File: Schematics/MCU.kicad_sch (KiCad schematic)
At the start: 28 parts, among them J1 Microsemi_FlashPro-JTAG-10, U1 STM32F405RGT6, Y1 8mhz

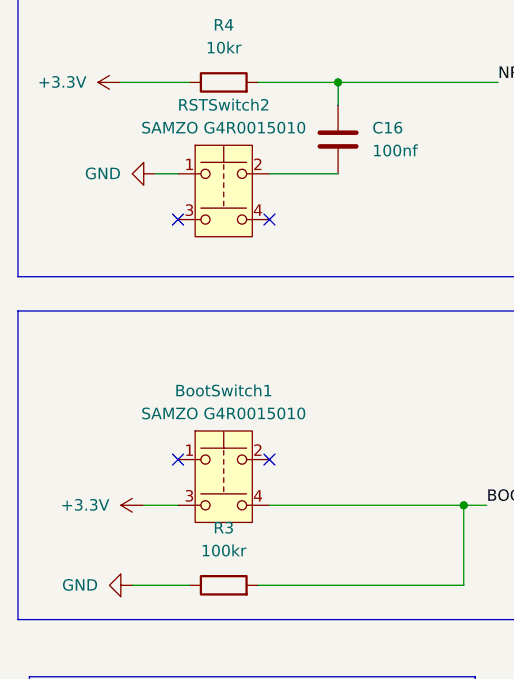
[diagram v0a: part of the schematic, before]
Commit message: fixed switch layout and unrouted nets
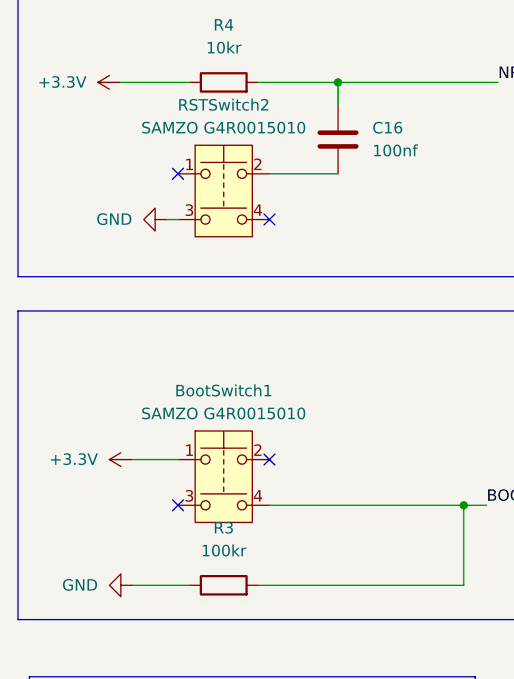
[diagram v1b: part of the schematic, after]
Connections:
- net +3.3V: now also BootSwitch1.1; no longer BootSwitch1.3
- net GND: now also RSTSwitch2.3; no longer RSTSwitch2.1
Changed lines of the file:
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@@
 	)
 	(no_connect
-		(at 33.02 95.25)
-	)
-	(no_connect
 		(at 127 96.52)
 	)
@@
 	)
 	(no_connect
+		(at 33.02 63.5)
+	)
+	(no_connect
 		(at 252.73 54.61)
 	)
@@
 	)
 	(no_connect
-		(at 33.02 68.58)
-	)
-	(no_connect
 		(at 127 121.92)
 	)
@@
 	)
 	(no_connect
+		(at 33.02 100.33)
+	)
+	(no_connect
 		(at 240.03 34.29)
 	)
@@
 	(wire
 		(pts
-			(xy 29.21 100.33) (xy 33.02 100.33)
+			(xy 29.21 157.48) (xy 31.75 157.48)
 		)
 		(stroke
@@
 	(wire
 		(pts
-			(xy 29.21 157.48) (xy 31.75 157.48)
+			(xy 31.75 68.58) (xy 33.02 68.58)
 		)
 		(stroke
@@
 	(wire
 		(pts
-			(xy 30.48 63.5) (xy 33.02 63.5)
-		)
-		(stroke
-			(width 0)
-			(type default)
-		)
-	)
-	(wire
-		(pts
 			(xy 153.67 31.75) (xy 160.02 31.75)
 		)
@@
 	(wire
 		(pts
+			(xy 27.94 95.25) (xy 33.02 95.25)
+		)
+		(stroke
+			(width 0)
+			(type default)
+		)
+	)
+	(wire
+		(pts
 			(xy 137.16 24.13) (xy 139.7 24.13)
 		)
@@
 	(symbol
 		(lib_id "power:+3.3V")
-		(at 29.21 100.33 90)
+		(at 27.94 95.25 90)
 		(unit 1)
 		(exclude_from_sim no)
@@
 		(fields_autoplaced yes)
 		(property "Reference" "#PWR017"
-			(at 33.02 100.33 0)
+			(at 31.75 95.25 0)
 			(effects
 				(font
@@
 		)
 		(property "Value" "+3.3V"
-			(at 25.4 100.3299 90)
+			(at 24.13 95.2499 90)
 			(effects
 				(font
@@
 		)
 		(property "Footprint" ""
-			(at 29.21 100.33 0)
+			(at 27.94 95.25 0)
 			(effects
 				(font
@@
 		)
 		(property "Datasheet" ""
-			(at 29.21 100.33 0)
+			(at 27.94 95.25 0)
 			(effects
 				(font
@@
 		)
 		(property "Description" "Power symbol creates a global label with name \"+3.3V\""
-			(at 29.21 100.33 0)
+			(at 27.94 95.25 0)
 			(effects
 				(font
@@
 	(symbol
 		(lib_id "power:GND")
-		(at 30.48 63.5 270)
+		(at 31.75 68.58 270)
 		(unit 1)
 		(exclude_from_sim no)
@@
 		(dnp no)
 		(property "Reference" "#PWR020"
-			(at 24.13 63.5 0)
+			(at 25.4 68.58 0)
 			(effects
 				(font
@@
 		)
 		(property "Value" "GND"
-			(at 26.67 63.4999 90)
+			(at 27.94 68.5799 90)
 			(effects
 				(font
@@
 		)
 		(property "Footprint" ""
-			(at 30.48 63.5 0)
+			(at 31.75 68.58 0)
 			(effects
 				(font
@@
 		)
 		(property "Datasheet" ""
-			(at 30.48 63.5 0)
+			(at 31.75 68.58 0)
 			(effects
 				(font
@@
 		)
 		(property "Description" "Power symbol creates a global label with name \"GND\" , ground"
-			(at 30.48 63.5 0)
+			(at 31.75 68.58 0)
 			(effects
 				(font

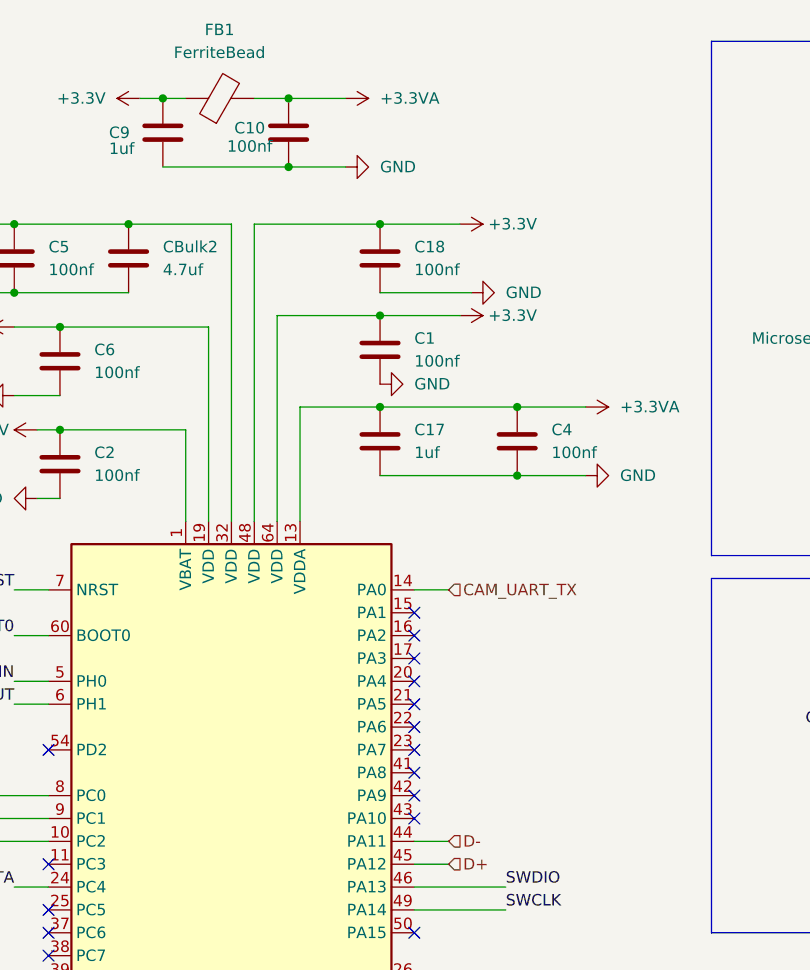
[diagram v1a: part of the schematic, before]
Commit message: Ran ERC added Pwr Flags
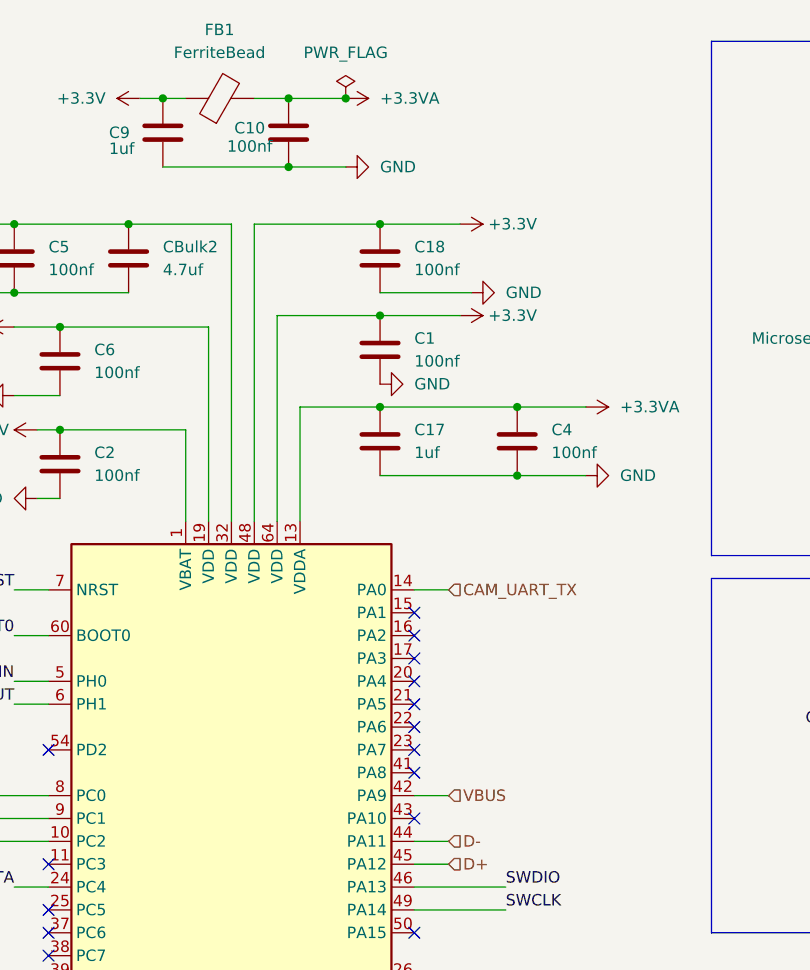
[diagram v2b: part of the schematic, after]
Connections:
- net VBUS: now reaches U1.42 (PA9)
- no-connect marks 47 -> 46
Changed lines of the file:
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@@
 	)
 	(junction
+		(at 160.02 24.13)
+		(diameter 0)
+		(color 0 0 0 0)
+	)
+	(junction
 		(at 128.27 49.53)
 		(diameter 0)
@@
 	)
 	(no_connect
-		(at 167.64 101.6)
-	)
-	(no_connect
 		(at 167.64 124.46)
 	)
@@
 	(wire
 		(pts
+			(xy 171.45 101.6) (xy 167.64 101.6)
+		)
+		(stroke
+			(width 0)
+			(type default)
+		)
+	)
+	(wire
+		(pts
 			(xy 123.19 57.15) (xy 128.27 57.15)
 		)
@@
 		)
 	)
+	(hierarchical_label "VBUS"
+		(shape input)
+		(at 171.45 101.6 0)
+		(effects
+			(font
+				(size 1.27 1.27)
+			)
+			(justify left)
+		)
+	)
 	(hierarchical_label "D-"
 		(shape input)
@@
 					(unit 1)
 				)
+			)
+		)
+	)
+	(symbol
+		(lib_id "power:PWR_FLAG")
+		(at 160.02 24.13 0)
+		(unit 1)
+		(exclude_from_sim no)
+		(in_bom yes)
+		(on_board yes)
+		(dnp no)
+		(fields_autoplaced yes)
+		(property "Reference" "#FLG03"
+			(at 160.02 22.225 0)
+			(effects
+				(font
+					(size 1.27 1.27)
+				)
+				(hide yes)
+			)
+		)
+		(property "Value" "PWR_FLAG"
+			(at 160.02 19.05 0)
+			(effects
+				(font
+					(size 1.27 1.27)
+				)
+			)
+		)
+		(property "Footprint" ""
+			(at 160.02 24.13 0)
+			(effects
+				(font
+					(size 1.27 1.27)
+				)
+				(hide yes)
+			)
+		)
+		(property "Datasheet" "~"
+			(at 160.02 24.13 0)
+			(effects
+				(font
+					(size 1.27 1.27)
+				)
+				(hide yes)
+			)
+		)
+		(property "Description" "Special symbol for telling ERC where power comes from"
+			(at 160.02 24.13 0)
+			(effects
+				(font
+					(size 1.27 1.27)
+				)
+				(hide yes)
+			)
+		)
+		(pin "1"
+		)
+		(instances
+			(project ""
+				(path "/65068a32-f105-4204-b50e-234054c5a6d0/5e494e8c-589b-4110-874f-f4b8b9240b86"
+					(reference "#FLG03")
+					(unit 1)
+				)

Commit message: ran DRC, passed awaiting final review
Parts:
- C19: LCSC C49393646 -> C49678
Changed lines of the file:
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@@
 			)
 		)
-		(property "LCSC" "C49393646"
+		(property "LCSC" "C49678"
 			(at 31.75 165.1 0)
 			(effects

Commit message: final design pcb
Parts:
- renumbered C19 to C1, C18 to C10, C1 to C11, C17 to C12, C4 to C13, C21 to C14, C22 to C15, C16 to C2, C7 to C3, C8 to C4, C2 to C7, C9 to C8, C10 to C9, CBulk2 to CBulk1, D3 to D1, R4 to R1, R3 to R2, R11 to R3, R12 to R4, RSTSwitch2 to RSTSwitch1
